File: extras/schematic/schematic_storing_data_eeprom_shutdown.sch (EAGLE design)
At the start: 21 parts, among them U1 SI4735-D60-GU

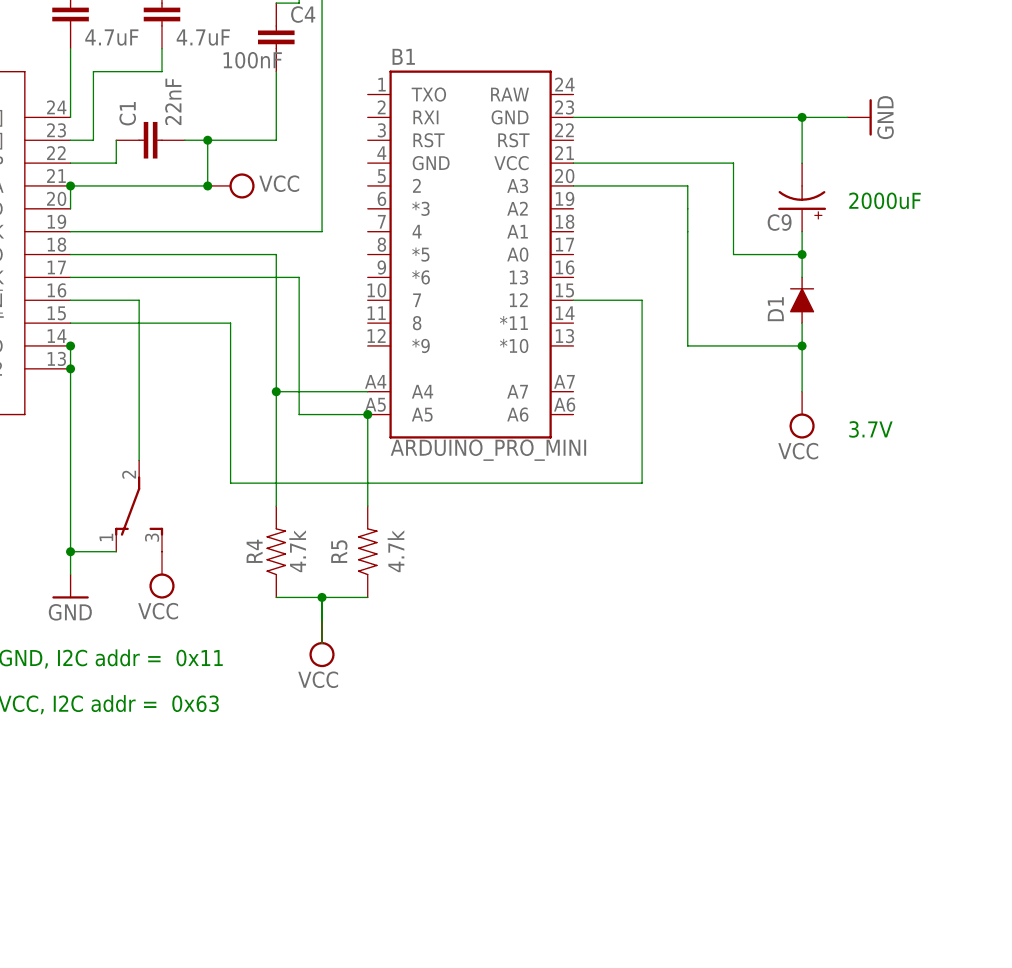
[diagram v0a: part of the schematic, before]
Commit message: SI473X Arduino Library
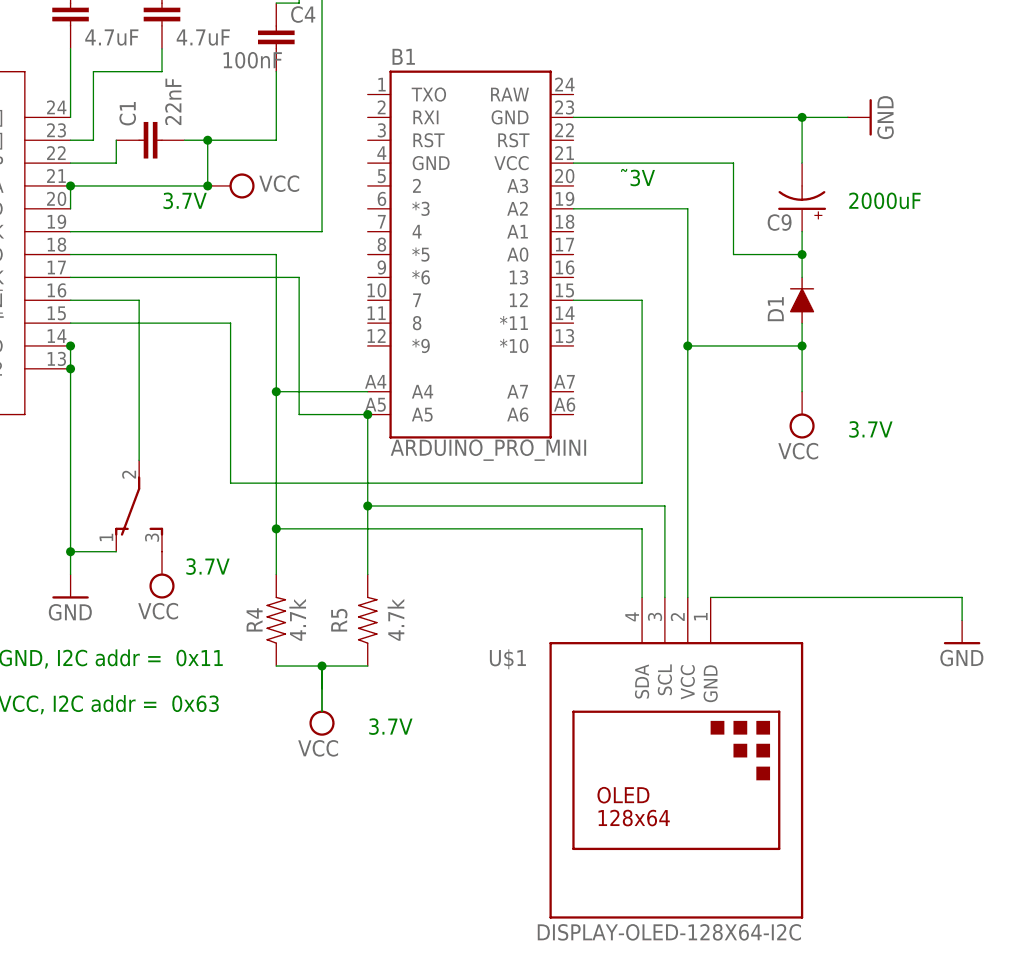
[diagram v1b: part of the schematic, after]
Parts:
- added U$1: DISPLAY-OLED-128X64-I2C, diy-modules:DISPLAY-OLED-128X64-I2C
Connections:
- net GND: now also U$1.GND
- net N$15: now also U$1.SDA
- net SDA: now also U$1.SCL
- net VCC: now also B1.A2, U$1.VCC; no longer B1.A3
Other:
- note added: "˜3V"
- moved on the sheet: R4, R5
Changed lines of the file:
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@@
 <part name="C9" library="SparkFun-Capacitors" library_urn="urn:adsk.eagle:library:510" deviceset="1000UF" device="-RADIAL-5MM-35V-20%-KIT" package3d_urn="urn:adsk.eagle:package:37421/1" value="1mf"/>
 <part name="D1" library="SparkFun-DiscreteSemi" library_urn="urn:adsk.eagle:library:514" deviceset="DIODE" device="-1N4148" package3d_urn="urn:adsk.eagle:package:38452/1" value="200mA/100V/1V"/>
+<part name="U$1" library="diy-modules" deviceset="DISPLAY-OLED-128X64-I2C" device=""/>
+<part name="GND2" library="supply1" library_urn="urn:adsk.eagle:library:371" deviceset="GND" device=""/>
 </parts>
 <sheets>
@@
 <text x="119.38" y="106.68" size="1.778" layer="91">2000uF</text>
 <text x="119.38" y="81.28" size="1.778" layer="91">3.7V</text>
+<text x="93.98" y="109.22" size="1.778" layer="91">˜3V</text>
+<text x="66.04" y="48.26" size="1.778" layer="91">3.7V</text>
+<text x="45.72" y="66.04" size="1.778" layer="91">3.7V</text>
+<text x="43.18" y="106.68" size="1.778" layer="91">3.7V</text>
 </plain>
 <instances>
@@
 <attribute name="VALUE" x="30.48" y="60.96" size="1.778" layer="96"/>
 </instance>
-<instance part="R4" gate="G$1" x="55.88" y="68.58" smashed="yes" rot="R90">
-<attribute name="NAME" x="54.356" y="68.58" size="1.778" layer="95" font="vector" rot="R90" align="bottom-center"/>
-<attribute name="VALUE" x="57.404" y="68.58" size="1.778" layer="96" font="vector" rot="R90" align="top-center"/>
-</instance>
-<instance part="R5" gate="G$1" x="66.04" y="68.58" smashed="yes" rot="R90">
-<attribute name="NAME" x="61.976" y="68.58" size="1.778" layer="95" font="vector" rot="R270" align="bottom-center"/>
-<attribute name="VALUE" x="70.104" y="68.58" size="1.778" layer="96" font="vector" rot="R270" align="top-center"/>
+<instance part="R4" gate="G$1" x="55.88" y="60.96" smashed="yes" rot="R90">
+<attribute name="NAME" x="54.356" y="60.96" size="1.778" layer="95" font="vector" rot="R90" align="bottom-center"/>
+<attribute name="VALUE" x="57.404" y="60.96" size="1.778" layer="96" font="vector" rot="R90" align="top-center"/>
+</instance>
+<instance part="R5" gate="G$1" x="66.04" y="60.96" smashed="yes" rot="R90">
+<attribute name="NAME" x="61.976" y="60.96" size="1.778" layer="95" font="vector" rot="R270" align="bottom-center"/>
+<attribute name="VALUE" x="70.104" y="60.96" size="1.778" layer="96" font="vector" rot="R270" align="top-center"/>
 </instance>
 <instance part="SUPPLY1" gate="G$1" x="50.8" y="109.22" smashed="yes" rot="R270">
@@
 <attribute name="VALUE" x="-60.96" y="83.82" size="1.778" layer="96"/>
 </instance>
-<instance part="SUPPLY3" gate="G$1" x="60.96" y="58.42" smashed="yes" rot="R180">
-<attribute name="VALUE" x="62.865" y="55.245" size="1.778" layer="96" rot="R180"/>
+<instance part="SUPPLY3" gate="G$1" x="60.96" y="50.8" smashed="yes" rot="R180">
+<attribute name="VALUE" x="62.865" y="47.625" size="1.778" layer="96" rot="R180"/>
 </instance>
 <instance part="S1" gate="BEF1" x="40.64" y="73.66" smashed="yes" rot="MR180"/>
@@
 <instance part="D1" gate="G$1" x="114.3" y="96.52" smashed="yes" rot="R90">
 <attribute name="NAME" x="112.268" y="93.98" size="1.778" layer="95" font="vector" rot="R90"/>
+</instance>
+<instance part="U$1" gate="G$1" x="99.06" y="43.18" smashed="yes" rot="MR0">
+<attribute name="NAME" x="83.82" y="55.88" size="1.778" layer="95" rot="MR0"/>
+<attribute name="VALUE" x="114.3" y="25.4" size="1.778" layer="96" rot="MR0"/>
+</instance>
+<instance part="GND2" gate="1" x="132.08" y="58.42" smashed="yes">
+<attribute name="VALUE" x="129.54" y="55.88" size="1.778" layer="96"/>
 </instance>
 </instances>
@@
 <junction x="-33.02" y="93.98"/>
 </segment>
+<segment>
+<pinref part="U$1" gate="G$1" pin="GND"/>
+<pinref part="GND2" gate="1" pin="GND"/>
+<wire x1="104.14" y1="63.5" x2="132.08" y2="63.5" width="0.1524" layer="91"/>
+<wire x1="132.08" y1="63.5" x2="132.08" y2="60.96" width="0.1524" layer="91"/>
+</segment>
 </net>
 <net name="SDA" class="0">
@@
 <pinref part="B1" gate="G$1" pin="A5"/>
 <wire x1="66.04" y1="83.82" x2="66.04" y2="73.66" width="0.1524" layer="91"/>
+<wire x1="66.04" y1="73.66" x2="66.04" y2="66.04" width="0.1524" layer="91"/>
 <wire x1="66.04" y1="83.82" x2="58.42" y2="83.82" width="0.1524" layer="91"/>
 <junction x="66.04" y="83.82"/>
@@
 <pinref part="U1" gate="A" pin="SCLK"/>
 <wire x1="58.42" y1="99.06" x2="33.02" y2="99.06" width="0.1524" layer="91"/>
+<pinref part="U$1" gate="G$1" pin="SCL"/>
+<wire x1="99.06" y1="63.5" x2="99.06" y2="73.66" width="0.1524" layer="91"/>
+<wire x1="99.06" y1="73.66" x2="66.04" y2="73.66" width="0.1524" layer="91"/>
+<junction x="66.04" y="73.66"/>
 </segment>
 </net>
@@
 <segment>
 <pinref part="R4" gate="G$1" pin="1"/>
-<wire x1="55.88" y1="63.5" x2="60.96" y2="63.5" width="0.1524" layer="91"/>
-<wire x1="60.96" y1="63.5" x2="60.96" y2="58.42" width="0.1524" layer="91"/>
+<wire x1="55.88" y1="55.88" x2="60.96" y2="55.88" width="0.1524" layer="91"/>
+<wire x1="60.96" y1="55.88" x2="60.96" y2="50.8" width="0.1524" layer="91"/>
 <pinref part="R5" gate="G$1" pin="1"/>
-<wire x1="66.04" y1="63.5" x2="60.96" y2="63.5" width="0.1524" layer="91"/>
-<junction x="60.96" y="63.5"/>
+<wire x1="66.04" y1="55.88" x2="60.96" y2="55.88" width="0.1524" layer="91"/>
+<junction x="60.96" y="55.88"/>
 <pinref part="SUPPLY3" gate="G$1" pin="VCC"/>
-<wire x1="60.96" y1="60.96" x2="60.96" y2="63.5" width="0.1524" layer="91"/>
+<wire x1="60.96" y1="53.34" x2="60.96" y2="55.88" width="0.1524" layer="91"/>
 </segment>
 <segment>
@@
 <wire x1="114.3" y1="91.44" x2="114.3" y2="86.36" width="0.1524" layer="91"/>
 <wire x1="114.3" y1="91.44" x2="101.6" y2="91.44" width="0.1524" layer="91"/>
-<wire x1="101.6" y1="91.44" x2="101.6" y2="104.14" width="0.1524" layer="91"/>
 <junction x="114.3" y="91.44"/>
-<pinref part="B1" gate="G$1" pin="A3"/>
-<wire x1="101.6" y1="104.14" x2="101.6" y2="106.68" width="0.1524" layer="91"/>
-<wire x1="88.9" y1="109.22" x2="101.6" y2="109.22" width="0.1524" layer="91"/>
-<wire x1="101.6" y1="109.22" x2="101.6" y2="106.68" width="0.1524" layer="91"/>
+<pinref part="B1" gate="G$1" pin="A2"/>
+<wire x1="88.9" y1="106.68" x2="101.6" y2="106.68" width="0.1524" layer="91"/>
+<wire x1="101.6" y1="106.68" x2="101.6" y2="91.44" width="0.1524" layer="91"/>
+<pinref part="U$1" gate="G$1" pin="VCC"/>
+<wire x1="101.6" y1="63.5" x2="101.6" y2="91.44" width="0.1524" layer="91"/>
+<junction x="101.6" y="91.44"/>
 </segment>
 </net>
@@
 <wire x1="55.88" y1="86.36" x2="66.04" y2="86.36" width="0.1524" layer="91"/>
 <pinref part="R4" gate="G$1" pin="2"/>
-<wire x1="55.88" y1="73.66" x2="55.88" y2="86.36" width="0.1524" layer="91"/>
+<wire x1="55.88" y1="66.04" x2="55.88" y2="71.12" width="0.1524" layer="91"/>
 <pinref part="U1" gate="A" pin="SDIO"/>
+<wire x1="55.88" y1="71.12" x2="55.88" y2="86.36" width="0.1524" layer="91"/>
 <wire x1="33.02" y1="101.6" x2="55.88" y2="101.6" width="0.1524" layer="91"/>
 <wire x1="55.88" y1="101.6" x2="55.88" y2="86.36" width="0.1524" layer="91"/>
 <junction x="55.88" y="86.36"/>
-</segment>
-</net>
+<pinref part="U$1" gate="G$1" pin="SDA"/>
+<wire x1="96.52" y1="63.5" x2="96.52" y2="71.12" width="0.1524" layer="91"/>
+<wire x1="96.52" y1="71.12" x2="55.88" y2="71.12" width="0.1524" layer="91"/>
+<junction x="55.88" y="71.12"/>
+</segment>
+</net>

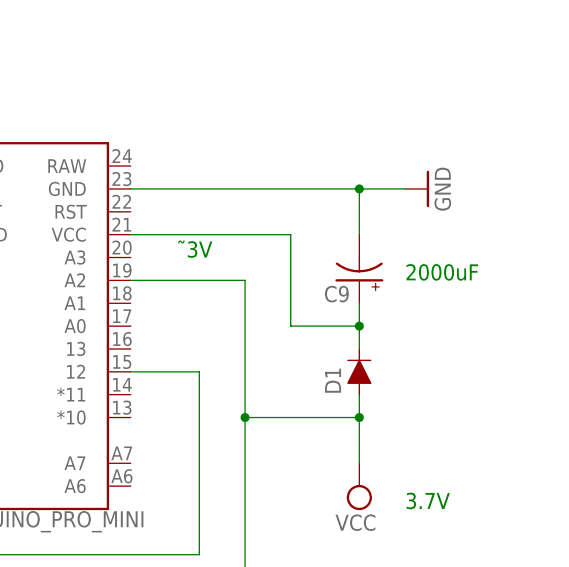
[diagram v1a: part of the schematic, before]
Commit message: SI473X Arduino Library
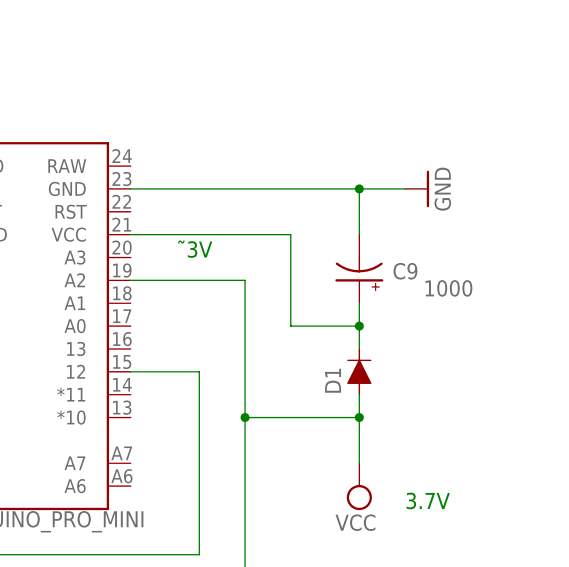
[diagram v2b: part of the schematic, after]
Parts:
- C9: UF (none) -> 1000
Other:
- note removed: "2000uF"
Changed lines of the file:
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@@
 <part name="S1" library="switch" library_urn="urn:adsk.eagle:library:380" deviceset="TL36WO" device="" package3d_urn="urn:adsk.eagle:package:27754/1"/>
 <part name="SUPPLY4" library="supply2" library_urn="urn:adsk.eagle:library:372" deviceset="VCC" device=""/>
-<part name="C9" library="SparkFun-Capacitors" library_urn="urn:adsk.eagle:library:510" deviceset="1000UF" device="-RADIAL-5MM-35V-20%-KIT" package3d_urn="urn:adsk.eagle:package:37421/1" value="1mf"/>
+<part name="C9" library="SparkFun-Capacitors" library_urn="urn:adsk.eagle:library:510" deviceset="1000UF" device="-RADIAL-5MM-35V-20%-KIT" package3d_urn="urn:adsk.eagle:package:37421/1" value="1mf">
+<attribute name="UF" value="1000"/>
+</part>
 <part name="D1" library="SparkFun-DiscreteSemi" library_urn="urn:adsk.eagle:library:514" deviceset="DIODE" device="-1N4148" package3d_urn="urn:adsk.eagle:package:38452/1" value="200mA/100V/1V"/>
 <part name="U$1" library="diy-modules" deviceset="DISPLAY-OLED-128X64-I2C" device=""/>
@@
 <text x="22.86" y="50.8" size="1.778" layer="91">If VCC, I2C addr =  0x63</text>
 <text x="-22.86" y="152.4" size="1.778" layer="91">Storing data automatically before turning the Arduino off</text>
-<text x="119.38" y="106.68" size="1.778" layer="91">2000uF</text>
 <text x="119.38" y="81.28" size="1.778" layer="91">3.7V</text>
 <text x="93.98" y="109.22" size="1.778" layer="91">˜3V</text>
@@
 </instance>
 <instance part="C9" gate="G$1" x="114.3" y="106.68" smashed="yes" rot="R180">
-<attribute name="NAME" x="113.284" y="106.045" size="1.778" layer="95" font="vector" rot="R180"/>
+<attribute name="NAME" x="120.904" y="108.585" size="1.778" layer="95" font="vector" rot="R180"/>
+<attribute name="UF" x="127" y="106.68" size="1.778" layer="96" rot="R180"/>
 </instance>
 <instance part="D1" gate="G$1" x="114.3" y="96.52" smashed="yes" rot="R90">

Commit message: SI473X Arduino Library
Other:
- note added: "Optional"
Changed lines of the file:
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@@
 <text x="45.72" y="66.04" size="1.778" layer="91">3.7V</text>
 <text x="43.18" y="106.68" size="1.778" layer="91">3.7V</text>
+<rectangle x1="-35.56" y1="137.16" x2="-20.32" y2="147.32" layer="205"/>
+<text x="-35.56" y="149.86" size="1.778" layer="205">Optional</text>
 </plain>
 <instances>
